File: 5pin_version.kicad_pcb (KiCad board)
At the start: 2 copper layers, 193 x 67 mm, 83 parts, among them J1 GSB1C411111DS1HR, J3 Conn_01x04_Pin, SW1 SW_Push, SW10 SW_Push, SW11 SW_Push, SW12 SW_Push, SW13 SW_Push, SW14 SW_Push, SW15 SW_Push, SW16 SW_Push, SW17 SW_Push, SW18 SW_Push, SW19 SW_Push, SW2 SW_Push, SW20 SW_Push, SW21 SW_Push, SW22 SW_Push, SW23 SW_Push, SW24 SW_Push, SW25 SW_Push, SW26 SW_Push, SW27 SW_Push, SW28 SW_Push, SW29 SW_Push, SW3 SW_Push, SW30 SW_Push, SW4 SW_Push, SW5 SW_Push, SW6 SW_Push, SW7 SW_Push, SW8 SW_Push, SW9 SW_Push, U1 TPS7B8133DRVR, U2 STM32L053C8T6

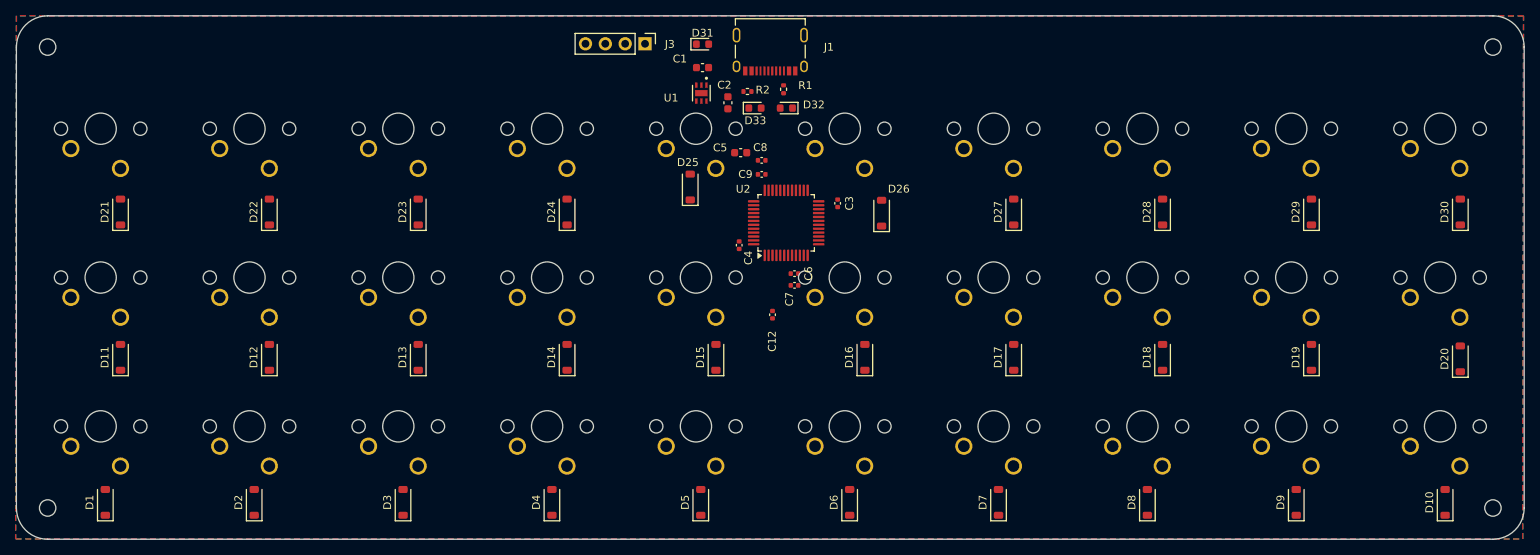
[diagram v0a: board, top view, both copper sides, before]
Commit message: rewired most lines, changed sizes to make easier to solder
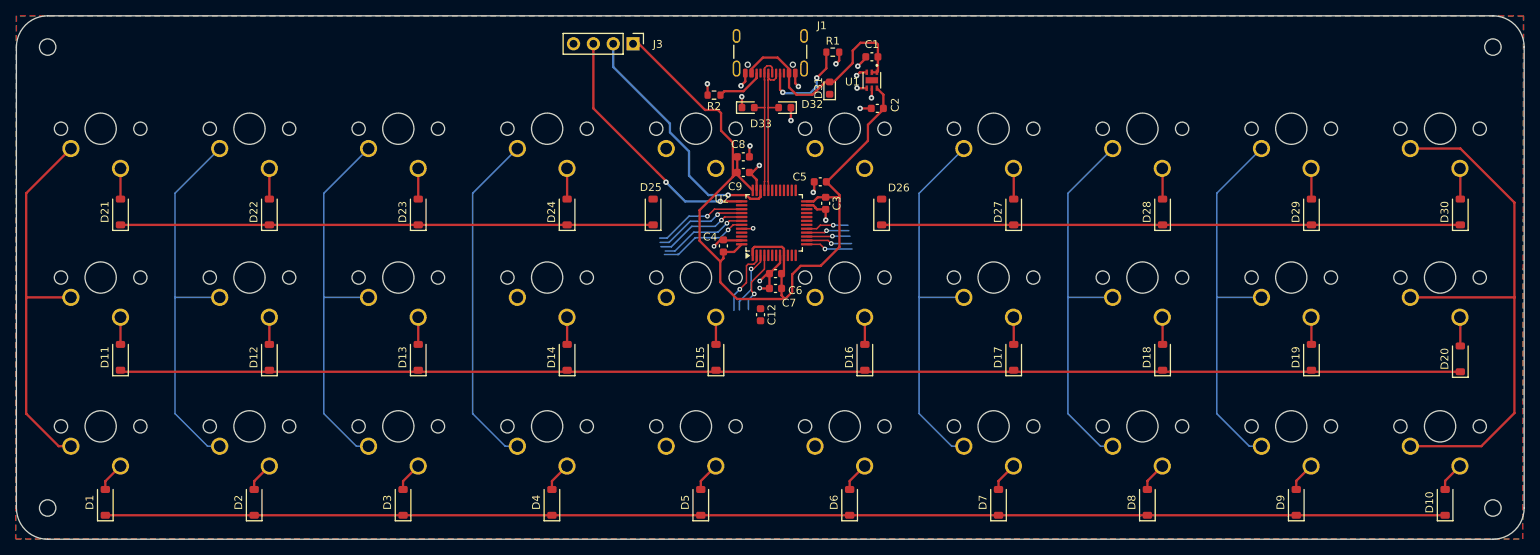
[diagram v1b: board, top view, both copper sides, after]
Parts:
- C12, C3, C4, C6, C7, C8, C9: footprint Capacitor_SMD:C_0402_1005Metric -> Capacitor_SMD:C_0603_1608Metric
- J1: value GSB1C411111DS1HR -> USB4105-GF-A; footprint usb_personal:AMPHENOL_GSB1C411111DS1HR -> Connector_USB:USB_C_Receptacle_GCT_USB4105-xx-A_16P_TopMnt_Horizontal
- R1, R2: footprint Resistor_SMD:R_0402_1005Metric -> Resistor_SMD:R_0603_1608Metric
- moved U1 21.9 mm to (168.2, 52.5)
- moved C1 21.7 mm to (168.2, 49.5)
- moved C2 19.1 mm to (168.8, 56.1), turned to 180 degrees
- moved D31 17.2 mm to (162.8, 53.5), turned to 90 degrees
- moved C5 10.9 mm to (161.6, 65.5)
- moved R1 7.89 mm to (163.2, 48.9), turned to 0 degrees
- moved D25 5.73 mm to (140.2, 69.3)
- moved R2 4.30 mm to (147.9, 54.4)
- moved C7 2.47 mm to (155.8, 79.1)
- moved C6 2.43 mm to (155.8, 77.2)
- moved C8 2.39 mm to (151.7, 62.3)
- moved C9 2.36 mm to (151.7, 64.3)
- moved C4 2.02 mm to (149.2, 73.7)
- moved C12 1.53 mm to (153.9, 82.5)
- moved C3 1.53 mm to (162.2, 68.2)
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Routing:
- net /matrix/ROW1: track 0.00 -> 177.1 mm, vias 0 -> 1
- net /matrix/ROW0: track 0.00 -> 177.0 mm, vias 0 -> 1
- net /matrix/ROW2: track 0.00 -> 142.2 mm
- net +3.3V: track 0.00 -> 111.0 mm
- net /matrix/COL9: track 0.00 -> 71.5 mm
- net /matrix/COL2: track 0.00 -> 61.4 mm, vias 0 -> 1
- net /matrix/COL1: track 0.00 -> 60.9 mm, vias 0 -> 1
- net /matrix/COL0: track 0.00 -> 58.2 mm, vias 0 -> 1
- net /matrix/COL3: track 0.00 -> 51.8 mm, vias 0 -> 1
- net /matrix/COL6: track 0.00 -> 49.5 mm
- net /matrix/COL7: track 0.00 -> 49.5 mm
- net /matrix/COL8: track 0.00 -> 49.5 mm
- net GND: track 0.00 -> 41.3 mm, vias 0 -> 19
- net /mcu/SWCLK: track 0.00 -> 32.3 mm, vias 0 -> 2
- net /mcu/SWDIO: track 0.00 -> 32.2 mm, vias 0 -> 1
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
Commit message: completed re-routing
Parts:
- turned D1 to -90 degrees
- turned D10 to -90 degrees
- turned D11 to -90 degrees
- turned D12 to -90 degrees
- turned D13 to -90 degrees
- turned D14 to -90 degrees
- turned D15 to -90 degrees
- turned D16 to -90 degrees
- turned D17 to -90 degrees
- turned D18 to -90 degrees
- turned D19 to -90 degrees
- turned D2 to -90 degrees
- turned D20 to -90 degrees
- turned D21 to -90 degrees
- turned D22 to -90 degrees
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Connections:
- D1 pad 1: /matrix/ROW0 -> Net-(D1-K)
- D1 pad 2: Net-(D1-A) -> /matrix/ROW0
- D10 pad 1: /matrix/ROW0 -> Net-(D10-K)
- D10 pad 2: Net-(D10-A) -> /matrix/ROW0
- D11 pad 1: /matrix/ROW1 -> Net-(D11-K)
- D11 pad 2: Net-(D11-A) -> /matrix/ROW1
- D12 pad 1: /matrix/ROW1 -> Net-(D12-K)
- D12 pad 2: Net-(D12-A) -> /matrix/ROW1
- D13 pad 1: /matrix/ROW1 -> Net-(D13-K)
- D13 pad 2: Net-(D13-A) -> /matrix/ROW1
- D14 pad 1: /matrix/ROW1 -> Net-(D14-K)
- D14 pad 2: Net-(D14-A) -> /matrix/ROW1
- D15 pad 1: /matrix/ROW1 -> Net-(D15-K)
- D15 pad 2: Net-(D15-A) -> /matrix/ROW1
- D16 pad 1: /matrix/ROW1 -> Net-(D16-K)
- D16 pad 2: Net-(D16-A) -> /matrix/ROW1
- D17 pad 1: /matrix/ROW1 -> Net-(D17-K)
- D17 pad 2: Net-(D17-A) -> /matrix/ROW1
- D18 pad 1: /matrix/ROW1 -> Net-(D18-K)
- D18 pad 2: Net-(D18-A) -> /matrix/ROW1
- D19 pad 1: /matrix/ROW1 -> Net-(D19-K)
- D19 pad 2: Net-(D19-A) -> /matrix/ROW1
- D2 pad 1: /matrix/ROW0 -> Net-(D2-K)
- D2 pad 2: Net-(D2-A) -> /matrix/ROW0
- D20 pad 1: /matrix/ROW1 -> Net-(D20-K)
- D20 pad 2: Net-(D20-A) -> /matrix/ROW1
- D21 pad 1: /matrix/ROW2 -> Net-(D21-K)
- D21 pad 2: Net-(D21-A) -> /matrix/ROW2
- D22 pad 1: /matrix/ROW2 -> Net-(D22-K)
- D22 pad 2: Net-(D22-A) -> /matrix/ROW2
- D23 pad 1: /matrix/ROW2 -> Net-(D23-K)
- D23 pad 2: Net-(D23-A) -> /matrix/ROW2
- D24 pad 1: /matrix/ROW2 -> Net-(D24-K)
- D24 pad 2: Net-(D24-A) -> /matrix/ROW2
- D25 pad 1: /matrix/ROW2 -> Net-(D25-K)
- D25 pad 2: Net-(D25-A) -> /matrix/ROW2
- D26 pad 1: /matrix/ROW2 -> Net-(D26-K)
- D26 pad 2: Net-(D26-A) -> /matrix/ROW2
- D27 pad 1: /matrix/ROW2 -> Net-(D27-K)
- D27 pad 2: Net-(D27-A) -> /matrix/ROW2
- D28 pad 1: /matrix/ROW2 -> Net-(D28-K)
- D28 pad 2: Net-(D28-A) -> /matrix/ROW2
- D29 pad 1: /matrix/ROW2 -> Net-(D29-K)
- D29 pad 2: Net-(D29-A) -> /matrix/ROW2
- D3 pad 1: /matrix/ROW0 -> Net-(D3-K)
- D3 pad 2: Net-(D3-A) -> /matrix/ROW0
- D30 pad 1: /matrix/ROW2 -> Net-(D30-K)
- D30 pad 2: Net-(D30-A) -> /matrix/ROW2
- D4 pad 1: /matrix/ROW0 -> Net-(D4-K)
- D4 pad 2: Net-(D4-A) -> /matrix/ROW0
- D5 pad 1: /matrix/ROW0 -> Net-(D5-K)
- D5 pad 2: Net-(D5-A) -> /matrix/ROW0
- D6 pad 1: /matrix/ROW0 -> Net-(D6-K)
- D6 pad 2: Net-(D6-A) -> /matrix/ROW0
- D7 pad 1: /matrix/ROW0 -> Net-(D7-K)
- D7 pad 2: Net-(D7-A) -> /matrix/ROW0
- D8 pad 1: /matrix/ROW0 -> Net-(D8-K)
- D8 pad 2: Net-(D8-A) -> /matrix/ROW0
- D9 pad 1: /matrix/ROW0 -> Net-(D9-K)
- D9 pad 2: Net-(D9-A) -> /matrix/ROW0
- SW1 pad 1: Net-(D1-A) -> Net-(D1-K)
- SW10 pad 1: Net-(D10-A) -> Net-(D10-K)
- SW11 pad 1: Net-(D11-A) -> Net-(D11-K)
- SW12 pad 1: Net-(D12-A) -> Net-(D12-K)
- SW13 pad 1: Net-(D13-A) -> Net-(D13-K)
- SW14 pad 1: Net-(D14-A) -> Net-(D14-K)
- SW15 pad 1: Net-(D15-A) -> Net-(D15-K)
- SW16 pad 1: Net-(D16-A) -> Net-(D16-K)
- SW17 pad 1: Net-(D17-A) -> Net-(D17-K)
- SW18 pad 1: Net-(D18-A) -> Net-(D18-K)
- SW19 pad 1: Net-(D19-A) -> Net-(D19-K)
- SW2 pad 1: Net-(D2-A) -> Net-(D2-K)
- SW20 pad 1: Net-(D20-A) -> Net-(D20-K)
- SW21 pad 1: Net-(D21-A) -> Net-(D21-K)
- SW22 pad 1: Net-(D22-A) -> Net-(D22-K)
- SW23 pad 1: Net-(D23-A) -> Net-(D23-K)
- SW24 pad 1: Net-(D24-A) -> Net-(D24-K)
- SW25 pad 1: Net-(D25-A) -> Net-(D25-K)
- SW26 pad 1: Net-(D26-A) -> Net-(D26-K)
- SW27 pad 1: Net-(D27-A) -> Net-(D27-K)
- SW28 pad 1: Net-(D28-A) -> Net-(D28-K)
- SW29 pad 1: Net-(D29-A) -> Net-(D29-K)
- SW3 pad 1: Net-(D3-A) -> Net-(D3-K)
- SW30 pad 1: Net-(D30-A) -> Net-(D30-K)
- SW4 pad 1: Net-(D4-A) -> Net-(D4-K)
- SW5 pad 1: Net-(D5-A) -> Net-(D5-K)
- SW6 pad 1: Net-(D6-A) -> Net-(D6-K)
- SW7 pad 1: Net-(D7-A) -> Net-(D7-K)
- SW8 pad 1: Net-(D8-A) -> Net-(D8-K)
- SW9 pad 1: Net-(D9-A) -> Net-(D9-K)
- U2 pad 13: unconnected-(U2-PA3-Pad13) -> /matrix/COL5
- U2 pad 14: unconnected-(U2-PA4-Pad14) -> /matrix/COL9
- U2 pad 15: unconnected-(U2-PA5-Pad15) -> /matrix/COL8
- U2 pad 16: /matrix/ROW0 -> /matrix/COL7
- U2 pad 17: /matrix/ROW1 -> /matrix/COL6
- U2 pad 2: /matrix/COL0 -> /matrix/ROW1
- U2 pad 25: /matrix/COL6 -> unconnected-(U2-PB12-Pad25)
- U2 pad 26: /matrix/COL5 -> unconnected-(U2-PB13-Pad26)
- U2 pad 27: /matrix/COL7 -> unconnected-(U2-PB14-Pad27)
- U2 pad 28: /matrix/COL8 -> unconnected-(U2-PB15-Pad28)
- U2 pad 29: /matrix/COL9 -> unconnected-(U2-PA8-Pad29)
- U2 pad 3: /matrix/COL4 -> /matrix/ROW0
- U2 pad 39: unconnected-(U2-PB3-Pad39) -> /matrix/COL0
- U2 pad 4: /matrix/COL3 -> unconnected-(U2-PC15-Pad4)
- U2 pad 40: unconnected-(U2-PB4-Pad40) -> /matrix/COL1
- U2 pad 42: /matrix/COL1 -> /matrix/COL3
- U2 pad 43: unconnected-(U2-PB7-Pad43) -> /matrix/COL4
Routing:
- net /matrix/COL0: track 58.2 -> 157.7 mm, vias 1 -> 2
- net /matrix/COL9: track 71.5 -> 152.5 mm, vias 0 -> 2
- net /matrix/COL1: track 60.9 -> 124.9 mm, vias 1 -> 2
- net /matrix/COL4: track 8.28 -> 65.2 mm, vias 1 -> 3
- net /matrix/COL8: track 49.5 -> 102.8 mm, vias 0 -> 3
- net /matrix/COL5: track 0.00 -> 43.4 mm, vias 0 -> 1
- net /matrix/COL2: track 61.4 -> 103.9 mm, vias 1 -> 2
- net /matrix/COL7: track 49.5 -> 83.4 mm, vias 0 -> 3
- net /matrix/ROW2: track 142.2 -> 174.6 mm, vias 0 -> 4
- net /matrix/ROW0: track 177.0 -> 207.8 mm, vias 1 -> 2
- net /matrix/COL3: track 51.8 -> 80.1 mm
- net /matrix/COL6: track 49.5 -> 64.1 mm, vias 0 -> 1
- net unconnected-(U2-PB3-Pad39): track 12.0 -> 0.00 mm, vias 1 -> 0
- net unconnected-(U2-PB4-Pad40): track 12.0 -> 0.00 mm, vias 1 -> 0
- net unconnected-(U2-PB7-Pad43): track 11.5 -> 0.00 mm, vias 1 -> 0
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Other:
- board text added: "3V3"
- board text added: "ANVIL"
- board text added: "CLK"
- board text added: "GND"
- board text added: "IO"

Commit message: board completed
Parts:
- D31: value 82306050029 -> PESD5V0S1BA,115; footprint Diode_SMD:D_0603_1608Metric -> Diode_SMD:D_SOD-323F
- D32, D33: value 82306050029 -> STS321050B100; footprint Diode_SMD:D_0603_1608Metric -> Diode_SMD:D_SOD-323F
- moved D31 0.30 mm to (162.8, 53.8)
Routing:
- net /mcu/NRST: track 0.00 -> 12.0 mm, vias 0 -> 2
- net /matrix/COL3: track 80.1 -> 85.7 mm
- net GND: track 41.3 -> 43.0 mm, vias 19 -> 49
- net +3.3V: track 111.0 -> 112.0 mm
